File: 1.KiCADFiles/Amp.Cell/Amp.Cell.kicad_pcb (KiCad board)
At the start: 4 copper layers, 20 x 40 mm, 19 parts, among them J4 Conn_01x08, Q1 MMBT3904, Q2 MMBT3906

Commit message: Cleaned Files
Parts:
- added G***: LOGO, 1.Logos:UTA, B.Cu at (22.1, 50.2)
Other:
- board text added: "Amp Cell v.1 July 2023 Alfredo Barajas Enriquez"

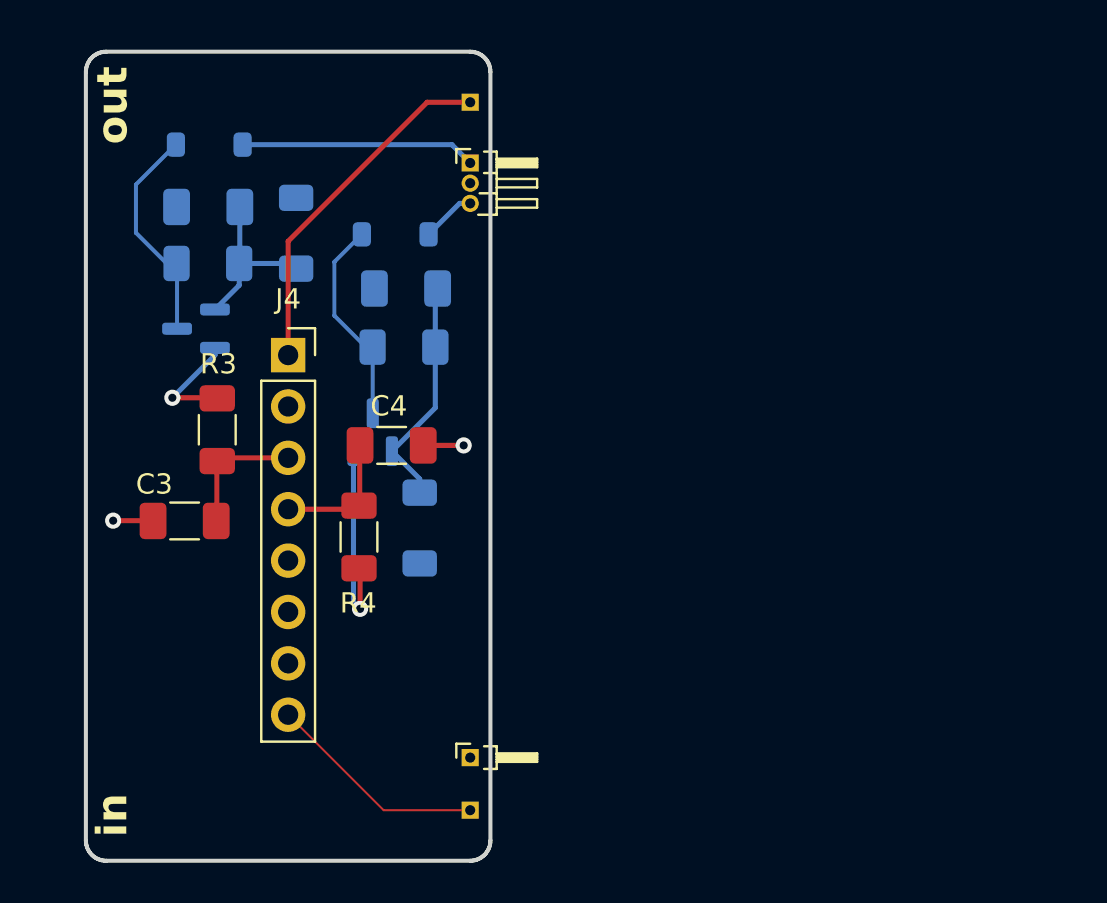
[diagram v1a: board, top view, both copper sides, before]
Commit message: Began adding signal traces, added cell holders
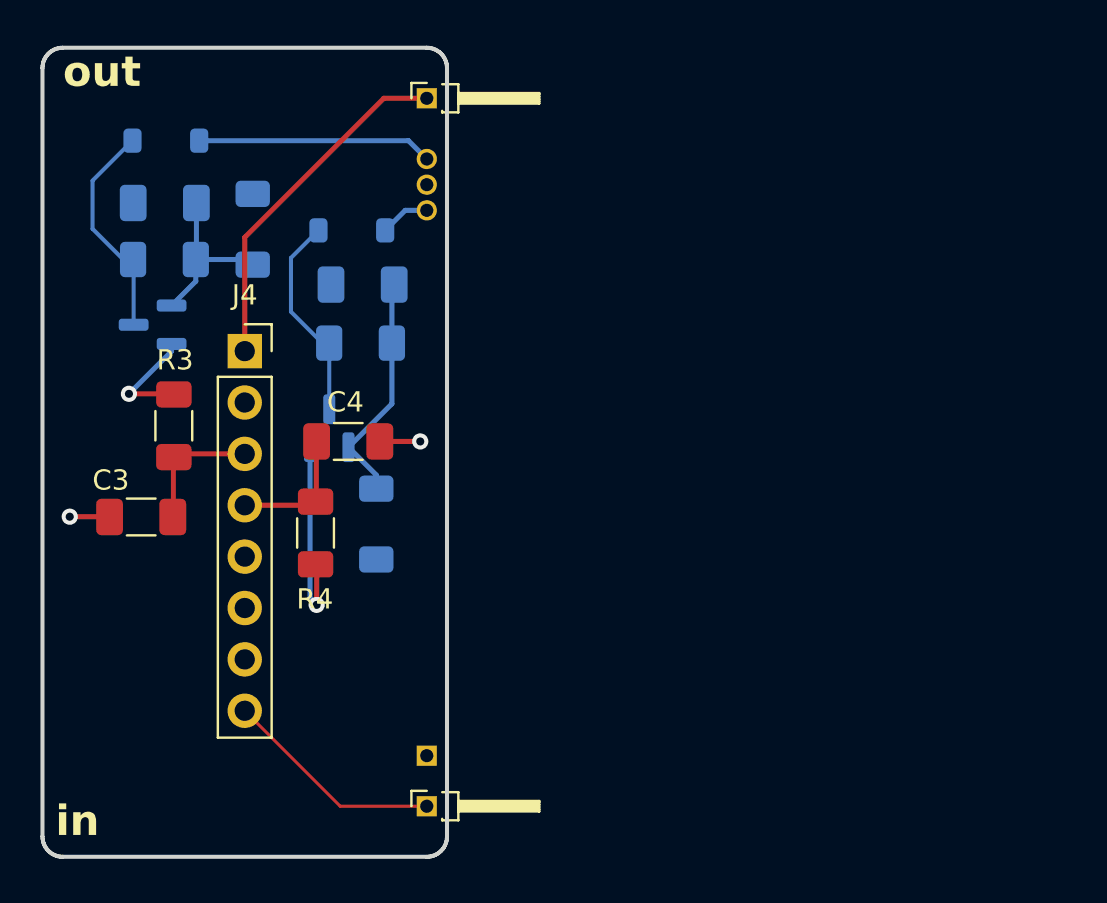
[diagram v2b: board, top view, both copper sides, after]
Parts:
- removed G***: LOGO, 1.Logos:UTA
- removed the REF** at (36.5, 50.6)
- removed the REF** at (36.5, 21.2)
- removed the REF** at (36.5, 18.2)
- removed the REF** at (36.5, 53.2)
- added REF**: PinHeader_1x01_P1.27mm_Horizontal, Connector_PinHeader_1.27mm:PinHeader_1x01_P1.27mm_Horizontal, F.Cu at (34.4, 18.0)
- added REF**: PinHeader_1x01_P1.27mm_Horizontal, Connector_PinHeader_1.27mm:PinHeader_1x01_P1.27mm_Horizontal, F.Cu at (34.4, 53.0)
- added REF**: PinHeader_1x01_P1.27mm_Horizontal, Connector_PinHeader_1.27mm:PinHeader_1x01_P1.27mm_Horizontal, B.Cu at (34.4, 50.5)
- added REF**: PinHeader_1x03_P1.27mm_Horizontal, Connector_PinHeader_1.27mm:PinHeader_1x03_P1.27mm_Horizontal, B.Cu at (34.4, 23.5)
- moved Q2 2.16 mm to (29.6, 34.3)
- moved C2 2.16 mm to (31.2, 27.2)
- moved D2 2.16 mm to (30.7, 24.5)
- moved J4 2.16 mm to (25.4, 30.5)
- moved R2 2.16 mm to (31.1, 30.1)
- moved R3 2.16 mm to (21.9, 34.2)
- moved R4 2.16 mm to (28.9, 39.5)
- moved D1 2.16 mm to (21.5, 20.1)
- moved D3 2.16 mm to (25.8, 24.5)
- moved R1 2.16 mm to (21.4, 25.9)
- moved C1 2.16 mm to (21.4, 23.2)
- moved C3 2.16 mm to (20.3, 38.7)
- moved Q1 2.16 mm to (20.8, 29.2)
- moved C4 2.16 mm to (30.5, 34.9)
- moved D4 2.16 mm to (31.9, 39.0)
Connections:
- D1 pad 2: Net-(D1-A) -> (no net)
- D2 pad 1: Net-(D2-K) -> (no net)
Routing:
- net (no net): track 0.00 -> 14.3 mm
- net Net-(D1-A): track 11.6 -> 0.00 mm
- net Net-(D2-K): track 2.88 -> 0.00 mm
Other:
- board text removed: "Amp Cell v.1 July 2023 Alfredo Barajas Enriquez"

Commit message: Updated Files
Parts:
- removed REF** (x3): PinHeader_1x01_P1.27mm_Horizontal, Connector_PinHeader_1.27mm:PinHeader_1x01_P1.27mm_Horizontal
- removed REF**: PinHeader_1x03_P1.27mm_Horizontal, Connector_PinHeader_1.27mm:PinHeader_1x03_P1.27mm_Horizontal
- added REF**10: PinHeader_1x02_P2.54mm_Horizontal, Connector_PinHeader_2.54mm:PinHeader_1x02_P2.54mm_Horizontal, F.Cu at (31.6, 39.4)
- added REF**11: PinHeader_1x03_P2.54mm_Horizontal, Connector_PinHeader_2.54mm:PinHeader_1x03_P2.54mm_Horizontal, F.Cu at (47.8, 39.4)
- added REF**12: PinHeader_1x02_P2.54mm_Horizontal, Connector_PinHeader_2.54mm:PinHeader_1x02_P2.54mm_Horizontal, F.Cu at (63.8, 39.4)
- moved D1 39.9 mm to (61.2, 24.2), turned to -90 degrees
- moved C1 36.7 mm to (58.1, 24.1), turned to 90 degrees
- moved R1 33.9 mm to (55.3, 24.1), turned to -90 degrees
- moved Q1 31.7 mm to (52.1, 23.5), turned to 90 degrees
- moved D3 31.3 mm to (56.8, 28.5), turned to 0 degrees
- moved D2 27.5 mm to (56.7, 33.4), turned to 90 degrees
- moved C3 27.3 mm to (42.6, 23.0), turned to 90 degrees
- moved R3 27.0 mm to (47.1, 24.6), turned to 180 degrees
- moved J4 25.5 mm to (50.8, 28.1), turned to -90 degrees
- moved C2 23.8 mm to (54.1, 33.9), turned to 90 degrees
- moved R2 20.4 mm to (51.2, 33.8), turned to -90 degrees
- moved Q2 17.5 mm to (47.0, 32.3), turned to 0 degrees
- moved C4 15.9 mm to (46.3, 33.2), turned to -90 degrees
- moved R4 15.1 mm to (41.8, 31.6), turned to 0 degrees
- moved D4 11.2 mm to (42.2, 34.6), turned to 0 degrees
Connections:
- D1 pad 2: (no net) -> +
- D2 pad 1: (no net) -> -
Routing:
- net +: track 0.00 -> 24.5 mm
- net -: track 0.00 -> 14.3 mm
- net (no net): track 14.3 -> 0.00 mm
- net Net-(J2-In): track 17.5 -> 20.0 mm
- net Net-(J3-In): track 11.0 -> 13.0 mm
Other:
- board size 20 x 40 mm -> 40 x 27 mm
